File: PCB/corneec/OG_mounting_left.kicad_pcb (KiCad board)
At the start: 2 copper layers, 133.8 x 91.4 mm, 53 parts, among them J1 OLED, J2 MJ-4PP-9, Q1 Q_NMOS_GSD, SW1 SW_Push, SW10 EC_SW, SW11 EC_SW, SW12 EC_SW, SW13 EC_SW, SW14 EC_SW, SW15 EC_SW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

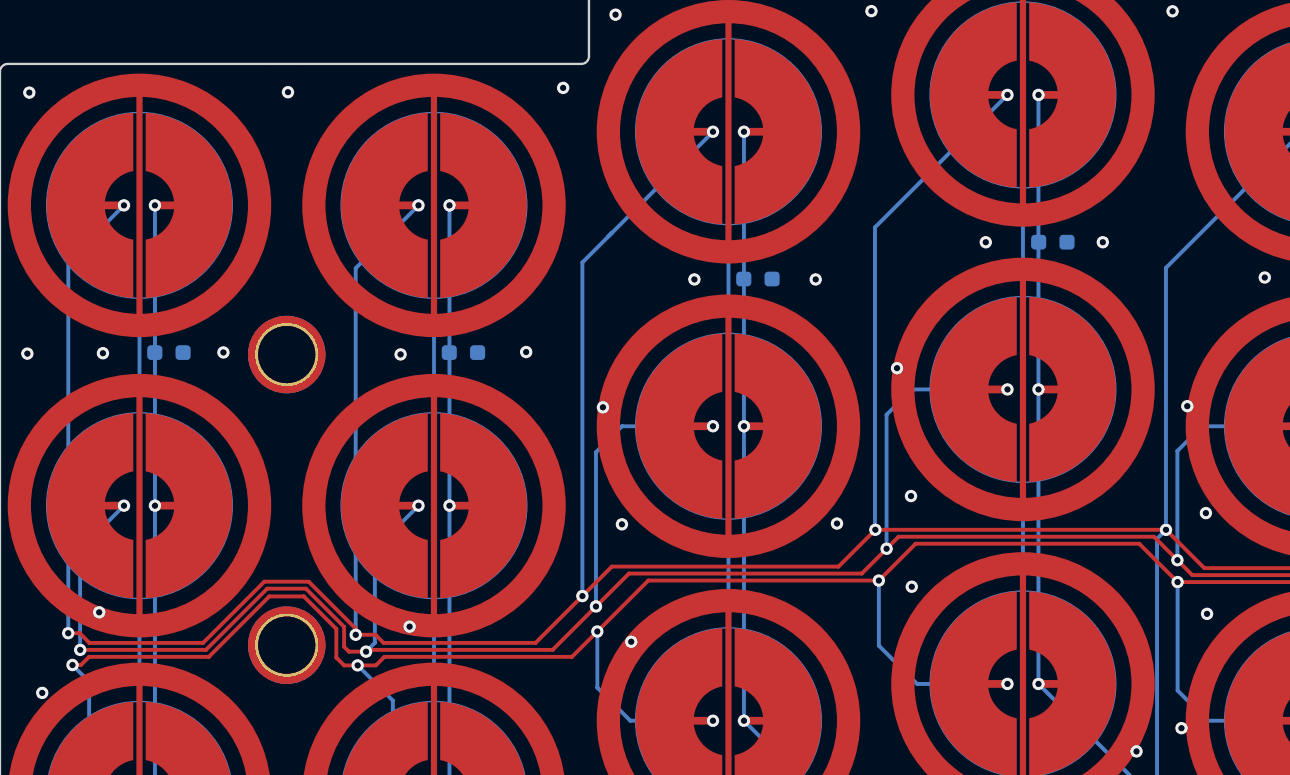
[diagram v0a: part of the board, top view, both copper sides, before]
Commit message: Update of rev commit to include extra screw mount
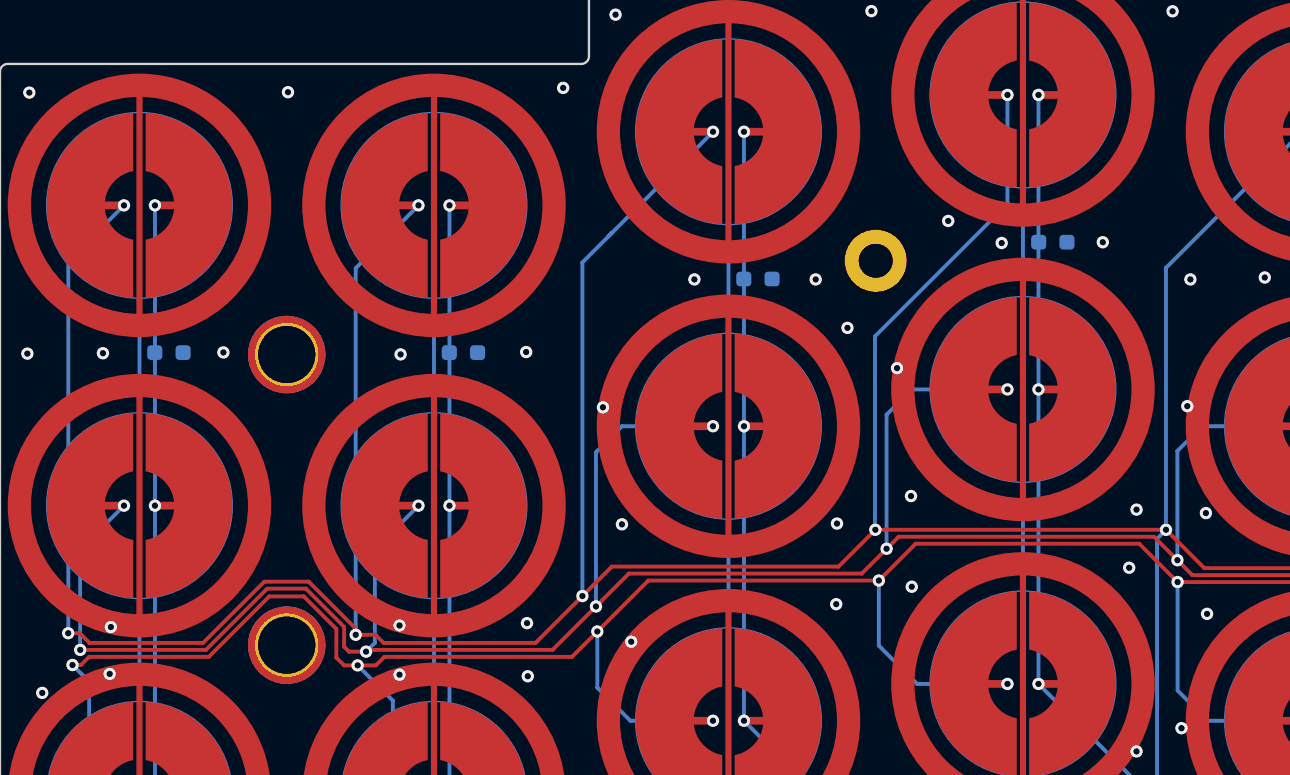
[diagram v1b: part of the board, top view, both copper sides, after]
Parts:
- added ?: , kbd:LEGO_HOLE, F.Cu at (128.5, 62.3)
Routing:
- net GNDA: vias 73 -> 83
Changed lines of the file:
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@@
       (drillshape 0)
       (scaleselection 1)
-      (outputdirectory "OG")
+      (outputdirectory "OG_left")
     )
   )
@@
     )
   )
+  (footprint "kbd:LEGO_HOLE" (layer "F.Cu")
+    (at 128.5236 62.2962)
+    (descr "Mounting Hole 2.2mm, no annular, M2")
+    (tags "mounting hole 2.2mm no annular m2")
+    (attr exclude_from_pos_files exclude_from_bom)
+    (fp_text reference "" (at 0 -3.2) (layer "F.SilkS")
+      (effects (font (size 1 1) (thickness 0.15)))
+    )
+    (fp_text value "" (at 0 3.2) (layer "F.Fab")
+      (effects (font (size 1 1) (thickness 0.15)))
+    )
+    (fp_text user "${REFERENCE}" (at 0.3 0) (layer "F.Fab")
+      (effects (font (size 1 1) (thickness 0.15)))
+    )
+    (fp_circle (center 0 0) (end 2.2 0) (layer "Cmts.User") (width 0.15) (fill none))
+    (fp_circle (center 0 0) (end 2.45 0) (layer "F.CrtYd") (width 0.05) (fill none))
+    (pad "" thru_hole circle locked (at 0 0) (size 4 4) (drill 2.2) (layers *.Cu *.Mask)
+      (net 1 "GNDA"))
+  )
   (footprint "cipulot_parts:HOLE_M2" (layer "F.Cu")
     (at 203.2736 105.8462)
@@
   (segment (start 167.525 98.85) (end 165.85 98.85) (width 0.25) (layer "F.Cu") (net 1))
   (via (at 158.3 100.725) (size 0.8) (drill 0.4) (layers "F.Cu" "B.Cu") (free) (net 1))
+  (via (at 97.8 89) (size 0.8) (drill 0.4) (layers "F.Cu" "B.Cu") (net 1))
   (via (at 97.8688 68.3366) (size 0.8) (drill 0.4) (layers "F.Cu" "B.Cu") (free) (net 1))
-  (via (at 98.45 85.9) (size 0.8) (drill 0.4) (layers "F.Cu" "B.Cu") (net 1))
+  (via (at 97.8 85.825) (size 0.8) (drill 0.4) (layers "F.Cu" "B.Cu") (net 1))
   (via (at 177.15 108.4) (size 0.8) (drill 0.4) (layers "F.Cu" "B.Cu") (free) (net 1))
   (via (at 199.95 102.75) (size 0.8) (drill 0.4) (layers "F.Cu" "B.Cu") (free) (net 1))
@@
   (via (at 147.675 46.2) (size 0.8) (drill 0.4) (layers "F.Cu" "B.Cu") (free) (net 1))
   (via (at 87.275 103.9) (size 0.8) (drill 0.4) (layers "F.Cu" "B.Cu") (free) (net 1))
+  (via (at 144.875 82.1) (size 0.8) (drill 0.4) (layers "F.Cu" "B.Cu") (free) (net 1))
   (via (at 88.325 99.425) (size 0.8) (drill 0.4) (layers "F.Cu" "B.Cu") (net 1))
   (via (at 132.25 108.825) (size 0.8) (drill 0.4) (layers "F.Cu" "B.Cu") (free) (net 1))
@@
   (via (at 130.85 83.325) (size 0.8) (drill 0.4) (layers "F.Cu" "B.Cu") (free) (net 1))
   (via (at 165.55 68.425) (size 0.8) (drill 0.4) (layers "F.Cu" "B.Cu") (free) (net 1))
+  (via (at 106.075 89.1) (size 0.8) (drill 0.4) (layers "F.Cu" "B.Cu") (free) (net 1))
   (via (at 184.15 86.875) (size 0.8) (drill 0.4) (layers "F.Cu" "B.Cu") (free) (net 1))
   (via (at 116.825 63.5) (size 0.8) (drill 0.4) (layers "F.Cu" "B.Cu") (free) (net 1))
+  (via (at 125.975 84.45) (size 0.8) (drill 0.4) (layers "F.Cu" "B.Cu") (free) (net 1))
   (via (at 184.15 82.75) (size 0.8) (drill 0.4) (layers "F.Cu" "B.Cu") (free) (net 1))
   (via (at 181.825 68.25) (size 0.8) (drill 0.4) (layers "F.Cu" "B.Cu") (free) (net 1))
+  (via (at 145.35 78.35) (size 0.8) (drill 0.4) (layers "F.Cu" "B.Cu") (free) (net 1))
   (via (at 130.8 77.475) (size 0.8) (drill 0.4) (layers "F.Cu" "B.Cu") (free) (net 1))
   (via (at 148.25 92.45) (size 0.8) (drill 0.4) (layers "F.Cu" "B.Cu") (free) (net 1))
@@
   (via (at 204.025 103.05) (size 0.8) (drill 0.4) (layers "F.Cu" "B.Cu") (free) (net 1))
   (via (at 144.55 97.925) (size 0.8) (drill 0.4) (layers "F.Cu" "B.Cu") (free) (net 1))
-  (via (at 78.425 84.975) (size 0.8) (drill 0.4) (layers "F.Cu" "B.Cu") (net 1))
+  (via (at 79.175 85.925) (size 0.8) (drill 0.4) (layers "F.Cu" "B.Cu") (net 1))
   (via (at 94.375 102.525) (size 0.8) (drill 0.4) (layers "F.Cu" "B.Cu") (net 1))
   (via (at 166.95 48.8) (size 0.8) (drill 0.4) (layers "F.Cu" "B.Cu") (free) (net 1))
-  (via (at 135.625 61.1) (size 0.8) (drill 0.4) (layers "F.Cu" "B.Cu") (free) (net 1))
+  (via (at 136.65 61.15) (size 0.8) (drill 0.4) (layers "F.Cu" "B.Cu") (free) (net 1))
   (via (at 203.775 108.85) (size 0.8) (drill 0.4) (layers "F.Cu" "B.Cu") (free) (net 1))
   (via (at 78.6664 68.2604) (size 0.8) (drill 0.4) (layers "F.Cu" "B.Cu") (free) (net 1))
   (via (at 110.925 71.75) (size 0.8) (drill 0.4) (layers "F.Cu" "B.Cu") (net 1))
+  (via (at 106.025 85.675) (size 0.8) (drill 0.4) (layers "F.Cu" "B.Cu") (free) (net 1))
   (via (at 111.7372 46.4164) (size 0.8) (drill 0.4) (layers "F.Cu" "B.Cu") (free) (net 1))
   (via (at 167.85 95.975) (size 0.8) (drill 0.4) (layers "F.Cu" "B.Cu") (net 1))
+  (via (at 148.825 63.5) (size 0.8) (drill 0.4) (layers "F.Cu" "B.Cu") (free) (net 1))
   (via (at 106.025 101.525) (size 0.8) (drill 0.4) (layers "F.Cu" "B.Cu") (net 1))
   (via (at 163.8 97.25) (size 0.8) (drill 0.4) (layers "F.Cu" "B.Cu") (free) (net 1))
   (via (at 166.8 76.6) (size 0.8) (drill 0.4) (layers "F.Cu" "B.Cu") (free) (net 1))
   (via (at 149.825 78.575) (size 0.8) (drill 0.4) (layers "F.Cu" "B.Cu") (free) (net 1))
+  (via (at 126.7 66.625) (size 0.8) (drill 0.4) (layers "F.Cu" "B.Cu") (free) (net 1))
   (via (at 145.35 93.95) (size 0.8) (drill 0.4) (layers "F.Cu" "B.Cu") (free) (net 1))
   (via (at 74.75 90.175) (size 0.8) (drill 0.4) (layers "F.Cu" "B.Cu") (free) (net 1))
+  (via (at 79.1 88.95) (size 0.8) (drill 0.4) (layers "F.Cu" "B.Cu") (net 1))
   (via (at 112.75 86.875) (size 0.8) (drill 0.4) (layers "F.Cu" "B.Cu") (net 1))
   (via (at 128.2472 46.1878) (size 0.8) (drill 0.4) (layers "F.Cu" "B.Cu") (free) (net 1))
@@
   (via (at 129.9 69.225) (size 0.8) (drill 0.4) (layers "F.Cu" "B.Cu") (net 1))
   (via (at 139.575 118.75) (size 0.8) (drill 0.4) (layers "F.Cu" "B.Cu") (free) (net 1))
+  (via (at 133.2 59.725) (size 0.8) (drill 0.4) (layers "F.Cu" "B.Cu") (free) (net 1))
   (via (at 198.625 111.225) (size 0.8) (drill 0.4) (layers "F.Cu" "B.Cu") (free) (net 1))
   (via (at 183.85 110.975) (size 0.8) (drill 0.4) (layers "F.Cu" "B.Cu") (free) (net 1))
@@
   (segment (start 146.675 95.925) (end 147.525 96.775) (width 0.25) (layer "B.Cu") (net 2))
   (segment (start 165.35 71.6) (end 175.0236 61.9264) (width 0.25) (layer "B.Cu") (net 2))
+  (segment (start 128.475 79.62692) (end 128.49904 79.65096) (width 0.25) (layer "B.Cu") (net 2))
   (segment (start 147.25 79.65) (end 147.25096 79.65096) (width 0.25) (layer "B.Cu") (net 2))
   (segment (start 147.25096 79.65096) (end 146.675 80.22692) (width 0.25) (layer "B.Cu") (net 2))
   (segment (start 99.0236 58.7212) (end 99.0236 58.7264) (width 0.25) (layer "B.Cu") (net 2))
   (segment (start 94.975 64.025) (end 94.975 86) (width 0.25) (layer "B.Cu") (net 2))
-  (segment (start 137.0236 51.5962) (end 128.475 60.1448) (width 0.25) (layer "B.Cu") (net 2))
   (segment (start 175.0236 61.9264) (end 175.0236 56.3462) (width 0.25) (layer "B.Cu") (net 2))
   (segment (start 99.0236 58.7264) (end 96.1 61.65) (width 0.25) (layer "B.Cu") (net 2))
-  (segment (start 128.475 79.62692) (end 128.475 60.1448) (width 0.25) (layer "B.Cu") (net 2))
   (segment (start 76.425 86.325) (end 76.4312 86.3188) (width 0.25) (layer "B.Cu") (net 2))
   (segment (start 147.25 62.75) (end 147.25 79.65) (width 0.25) (layer "B.Cu") (net 2))
   (segment (start 156.0236 53.9764) (end 147.25 62.75) (width 0.25) (layer "B.Cu") (net 2))
   (segment (start 147.5236 102.4514) (end 147.5236 110.5962) (width 0.25) (layer "B.Cu") (net 2))
+  (segment (start 137.0236 58.6264) (end 128.475 67.175) (width 0.25) (layer "B.Cu") (net 2))
   (segment (start 146.675 80.22692) (end 146.675 95.925) (width 0.25) (layer "B.Cu") (net 2))
   (segment (start 76.4312 86.3188) (end 76.4312 62.3136) (width 0.25) (layer "B.Cu") (net 2))
-  (segment (start 128.49904 79.65096) (end 128.475 79.62692) (width 0.25) (layer "B.Cu") (net 2))
   (segment (start 96.1 61.65) (end 94.975 62.775) (width 0.25) (layer "B.Cu") (net 2))
+  (segment (start 137.0236 51.5962) (end 137.0236 58.6264) (width 0.25) (layer "B.Cu") (net 2))
   (segment (start 76.4312 62.3136) (end 80.0236 58.7212) (width 0.25) (layer "B.Cu") (net 2))
   (segment (start 156.0236 53.9712) (end 156.0236 53.9764) (width 0.25) (layer "B.Cu") (net 2))
   (segment (start 118.0236 53.9764) (end 111.4875 60.5125) (width 0.25) (layer "B.Cu") (net 2))
   (segment (start 147.525 102.45) (end 147.5236 102.4514) (width 0.25) (layer "B.Cu") (net 2))
+  (segment (start 128.475 67.175) (end 128.475 79.62692) (width 0.25) (layer "B.Cu") (net 2))
   (segment (start 118.0236 53.9712) (end 118.0236 53.9764) (width 0.25) (layer "B.Cu") (net 2))
   (segment (start 94.975 86) (end 94.975 86.425) (width 0.25) (layer "B.Cu") (net 2))

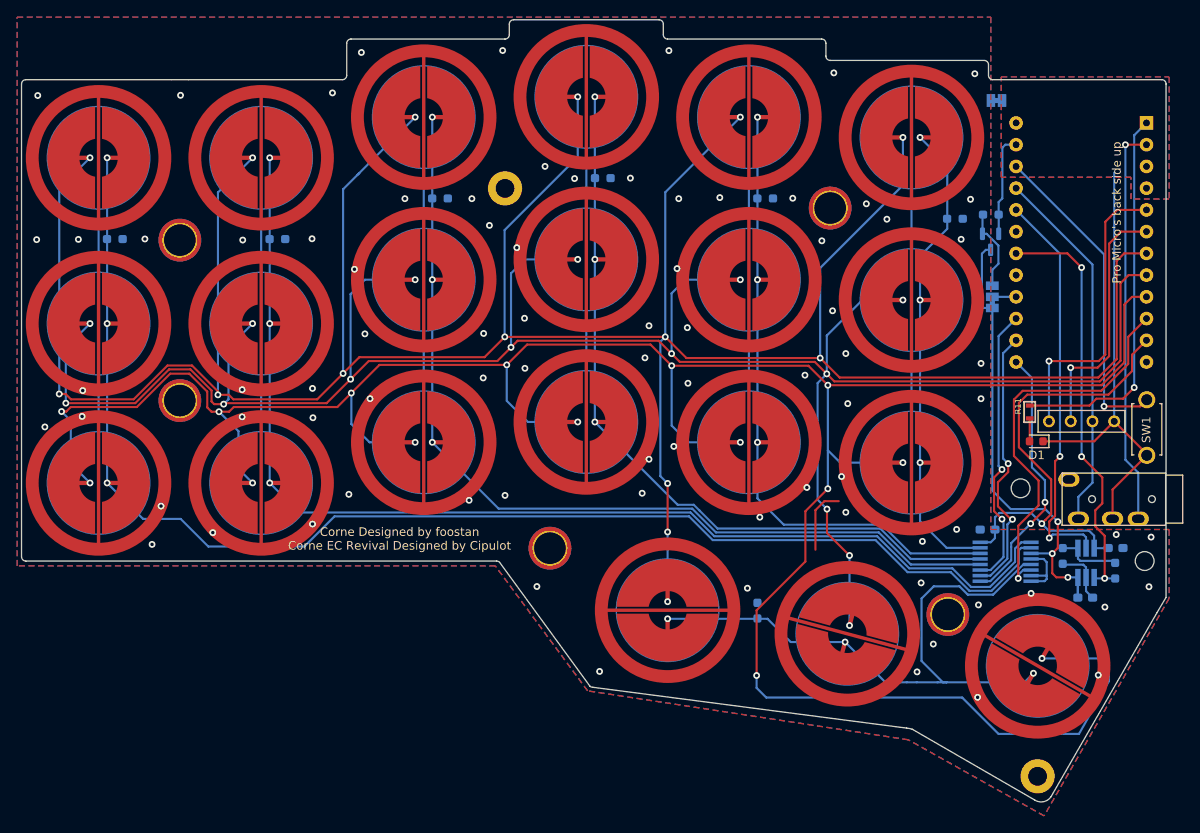
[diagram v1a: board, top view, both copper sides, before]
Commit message: Updated EC pad footprint
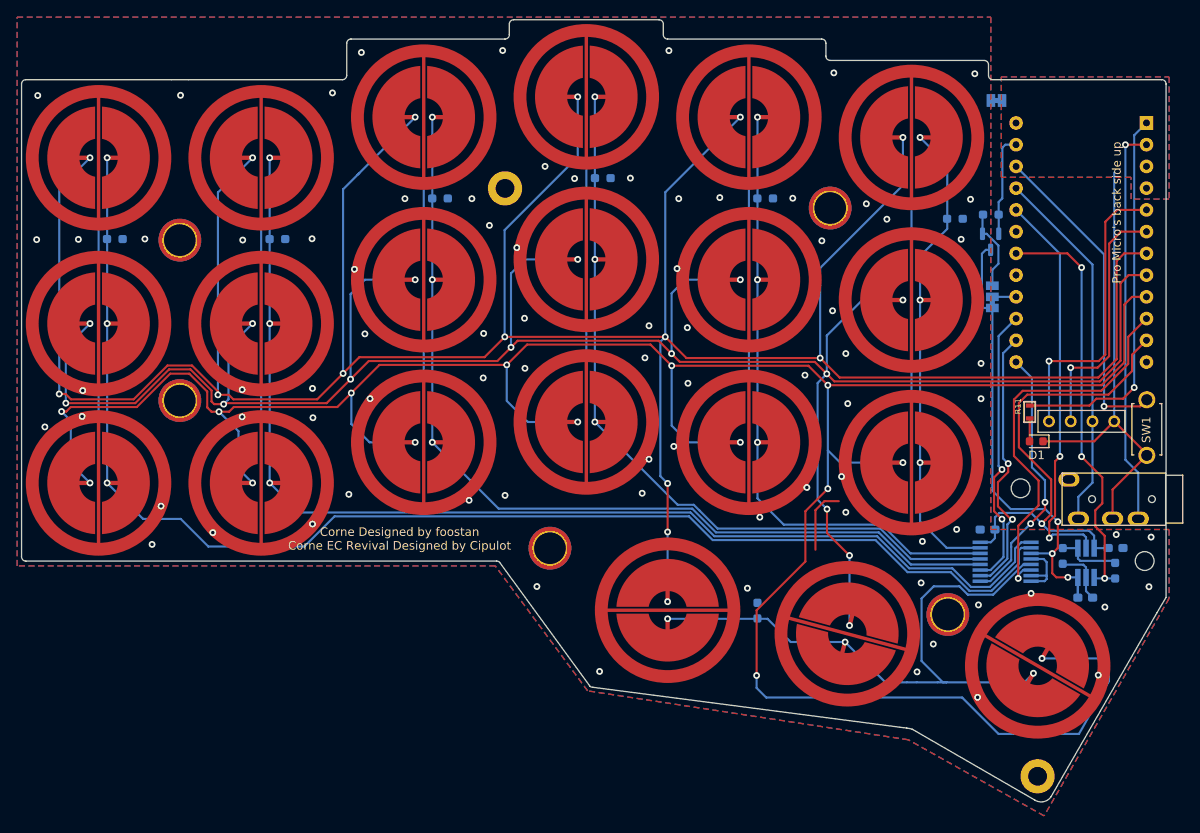
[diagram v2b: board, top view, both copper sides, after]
